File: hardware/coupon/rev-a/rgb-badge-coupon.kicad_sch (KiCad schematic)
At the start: 0 parts

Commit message: Connect provisional app switch and 3V3 converter
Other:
- added sheet Application 3V3 converter (provisional) (3v3-converter.kicad_sch)
- added sheet Application switch control (provisional) (app-control.kicad_sch)
- note added: "USB logic plus application switch/3V3 staged; SYS source, charger, gauge isolation and VLED pending."
- note removed: "USB data/detectors/logic captured; input protection, startup inhibition, charging and switched rails remain pending."
- title: Coupon Rev A - display, controller, USB logic and staged gauge -> Coupon Rev A - display, USB and provisional application power
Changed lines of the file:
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@@
 (generator_version "1.0")
 (paper "A3")
-(title_block (title "Coupon Rev A - display, controller, USB logic and staged gauge") (rev "A-draft") (comment 1 "SPDX-License-Identifier: CERN-OHL-S-2.0") (comment 2 "Input protection, charging, gauge switch and switched power pending"))
+(title_block (title "Coupon Rev A - display, USB and provisional application power") (rev "A-draft") (comment 1 "SPDX-License-Identifier: CERN-OHL-S-2.0") (comment 2 "Input protection, charger, gauge switch and VLED power pending"))
 (text "16 x 16 RGB matrix, TLC59581 driver, row selectors and ESP32-S3 controller" (at 20.32 20.32 0) (effects (font (size 2.0 2.0)) (justify left)))
 (text "Four sheets use global nets: ROW_00_A..ROW_15_A and COL_00_R/G/B..COL_15_R/G/B." (at 20.32 30.48 0) (effects (font (size 1.27 1.27)) (justify left)))
 (text "These are 16 switched anodes and 48 cathode sinks. They are not logic control signals." (at 20.32 38.10 0) (effects (font (size 1.27 1.27)) (justify left)))
-(text "USB data/detectors/logic captured; input protection, startup inhibition, charging and switched rails remain pending." (at 20.32 45.72 0) (effects (font (size 1.27 1.27)) (justify left)))
-(text "No PCB yet. QBLP1515 rotation: ADR 0008. Never fabricate before Gate A." (at 20.32 231.14 0) (effects (font (size 1.27 1.27)) (justify left)))
+(text "USB logic plus application switch/3V3 staged; SYS source, charger, gauge isolation and VLED pending." (at 20.32 45.72 0) (effects (font (size 1.27 1.27)) (justify left)))
+(text "No PCB yet. QBLP1515 rotation: ADR 0008. Never fabricate before Gate A." (at 20.32 273.05 0) (effects (font (size 1.27 1.27)) (justify left)))
 (sheet (at 20.32 63.50) (size 116.84 27.94)
 (exclude_from_sim no) (in_bom yes) (on_board yes) (dnp no)
@@
 (property "Sheetfile" "gauge.kicad_sch" (at 284.48 133.35 0) (effects (font (size 1.27 1.27)) (justify left top)))
 (instances (project "rgb-badge-coupon" (path "/207fb68e-2ddb-46bb-8712-eba2f8c5eef6" (page "12")))))
+(sheet (at 284.48 63.50) (size 116.84 22.86)
+(exclude_from_sim no) (in_bom yes) (on_board yes) (dnp no)
+(stroke (width 0.1524) (type solid)) (fill (color 0 0 0 0))
+(property "Sheetname" "Application switch control (provisional)" (at 284.48 62.23 0) (effects (font (size 1.27 1.27)) (justify left bottom)))
+(property "Sheetfile" "app-control.kicad_sch" (at 284.48 87.63 0) (effects (font (size 1.27 1.27)) (justify left top)))
+(instances (project "rgb-badge-coupon" (path "/207fb68e-2ddb-46bb-8712-eba2f8c5eef6" (page "13")))))
+(sheet (at 20.32 233.68) (size 116.84 22.86)
+(exclude_from_sim no) (in_bom yes) (on_board yes) (dnp no)
+(stroke (width 0.1524) (type solid)) (fill (color 0 0 0 0))
+(property "Sheetname" "Application 3V3 converter (provisional)" (at 20.32 232.41 0) (effects (font (size 1.27 1.27)) (justify left bottom)))
+(property "Sheetfile" "3v3-converter.kicad_sch" (at 20.32 257.81 0) (effects (font (size 1.27 1.27)) (justify left top)))
+(instances (project "rgb-badge-coupon" (path "/207fb68e-2ddb-46bb-8712-eba2f8c5eef6" (page "14")))))
 (sheet_instances (path "/" (page "1")))
 (embedded_fonts no)

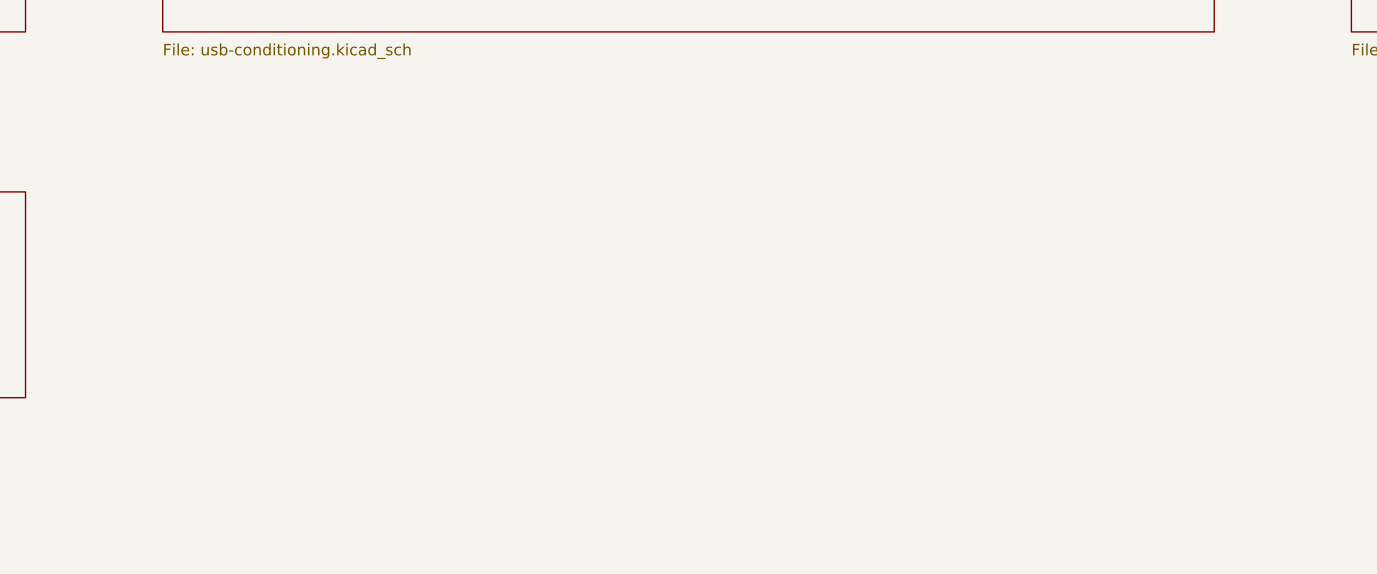
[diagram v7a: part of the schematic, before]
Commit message: Connect battery-facing charger temperature subcircuit
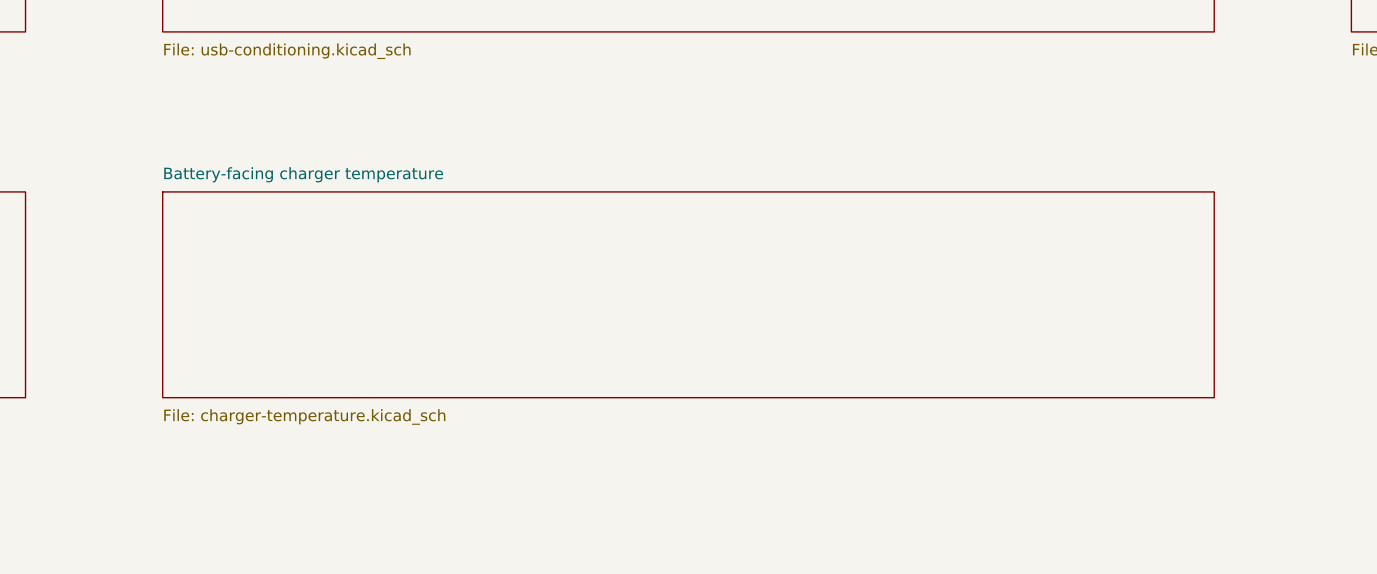
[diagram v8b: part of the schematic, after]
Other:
- added sheet Battery-facing charger temperature (charger-temperature.kicad_sch)
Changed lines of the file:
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@@
 (property "Sheetfile" "3v3-converter.kicad_sch" (at 20.32 257.81 0) (effects (font (size 1.27 1.27)) (justify left top)))
 (instances (project "rgb-badge-coupon" (path "/207fb68e-2ddb-46bb-8712-eba2f8c5eef6" (page "14")))))
+(sheet (at 152.40 233.68) (size 116.84 22.86)
+(exclude_from_sim no) (in_bom yes) (on_board yes) (dnp no)
+(stroke (width 0.1524) (type solid)) (fill (color 0 0 0 0))
+(property "Sheetname" "Battery-facing charger temperature" (at 152.40 232.41 0) (effects (font (size 1.27 1.27)) (justify left bottom)))
+(property "Sheetfile" "charger-temperature.kicad_sch" (at 152.40 257.81 0) (effects (font (size 1.27 1.27)) (justify left top)))
+(instances (project "rgb-badge-coupon" (path "/207fb68e-2ddb-46bb-8712-eba2f8c5eef6" (page "15")))))
 (sheet_instances (path "/" (page "1")))
 (embedded_fonts no)
